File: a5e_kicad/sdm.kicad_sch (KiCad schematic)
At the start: 22 parts, among them U2 W25X20CLZP, U7 A5EB013B-B23B

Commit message: savegame
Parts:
- removed U2: W25X20CLZP, Package_SON:WSON-8-1EP_6x5mm_P1.27mm_EP3.4x4.3mm, symbol Memory_Flash:W25X20CLZP
- added U2: IS25WP256D-xM, Package_SO:SOIC-16W_7.5x10.3mm_P1.27mm, symbol Memory_Flash:IS25WP256D-xM
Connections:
- net 1V8: now also U2.2 (VCC)
- net GND: now also U2.10 (GND)
- net qspi_CLK: now also U2.16 (SCK)
- net qspi_D0: now also U2.15 (SI/IO0)
- net qspi_D1: now also U2.8 (SO/IO1)
- net qspi_D2: now also U2.9 (~{WP}/IO2)
- net qspi_D3: now also U2.1 (~{HOLD}/IO3)
- net ~{qspi_CS}: now also U2.7 (~{CE})
- net ~{qspi_rst_n}: now also U2.3 (~{RESET}/NC)

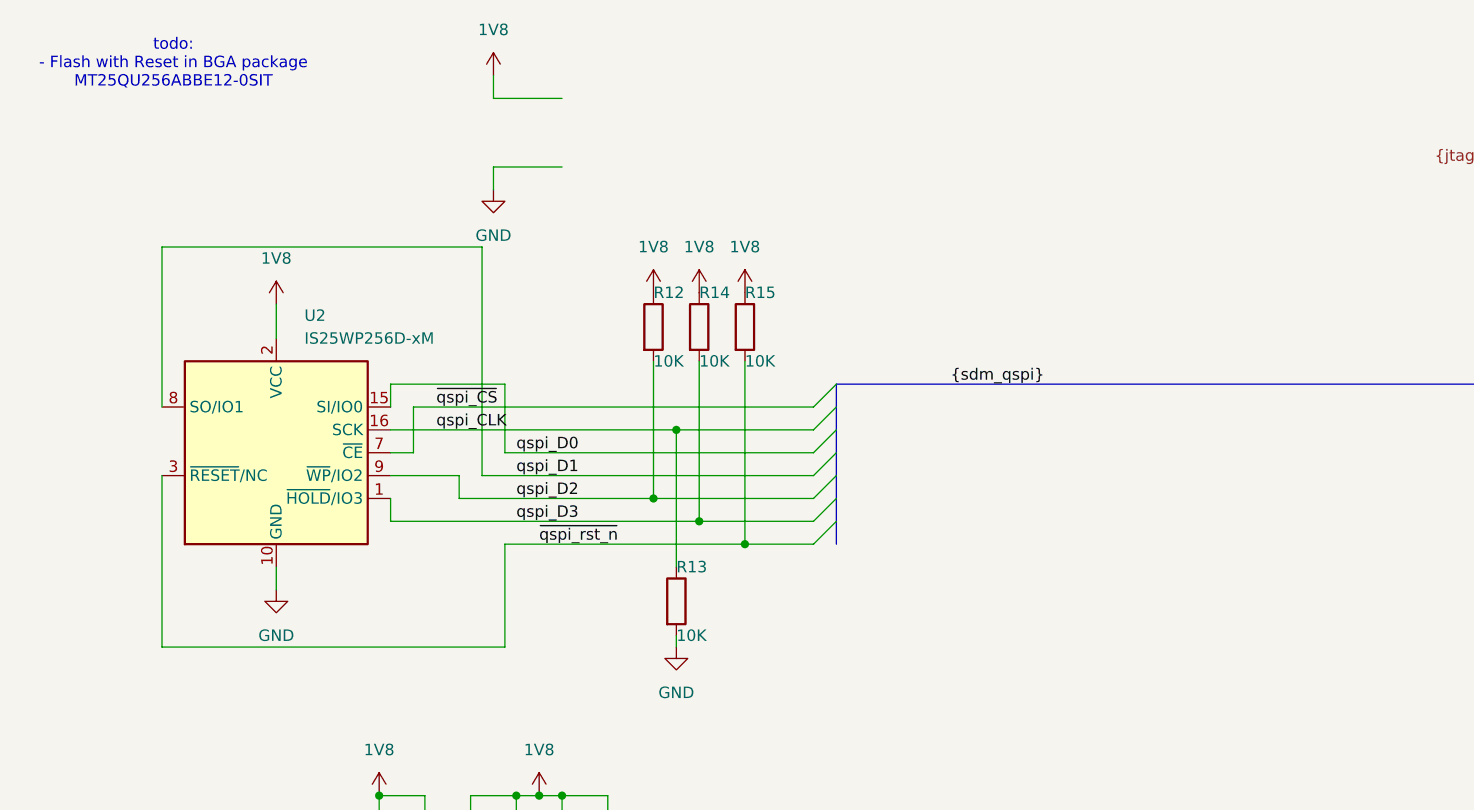
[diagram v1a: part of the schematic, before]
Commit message: change flash to correct part
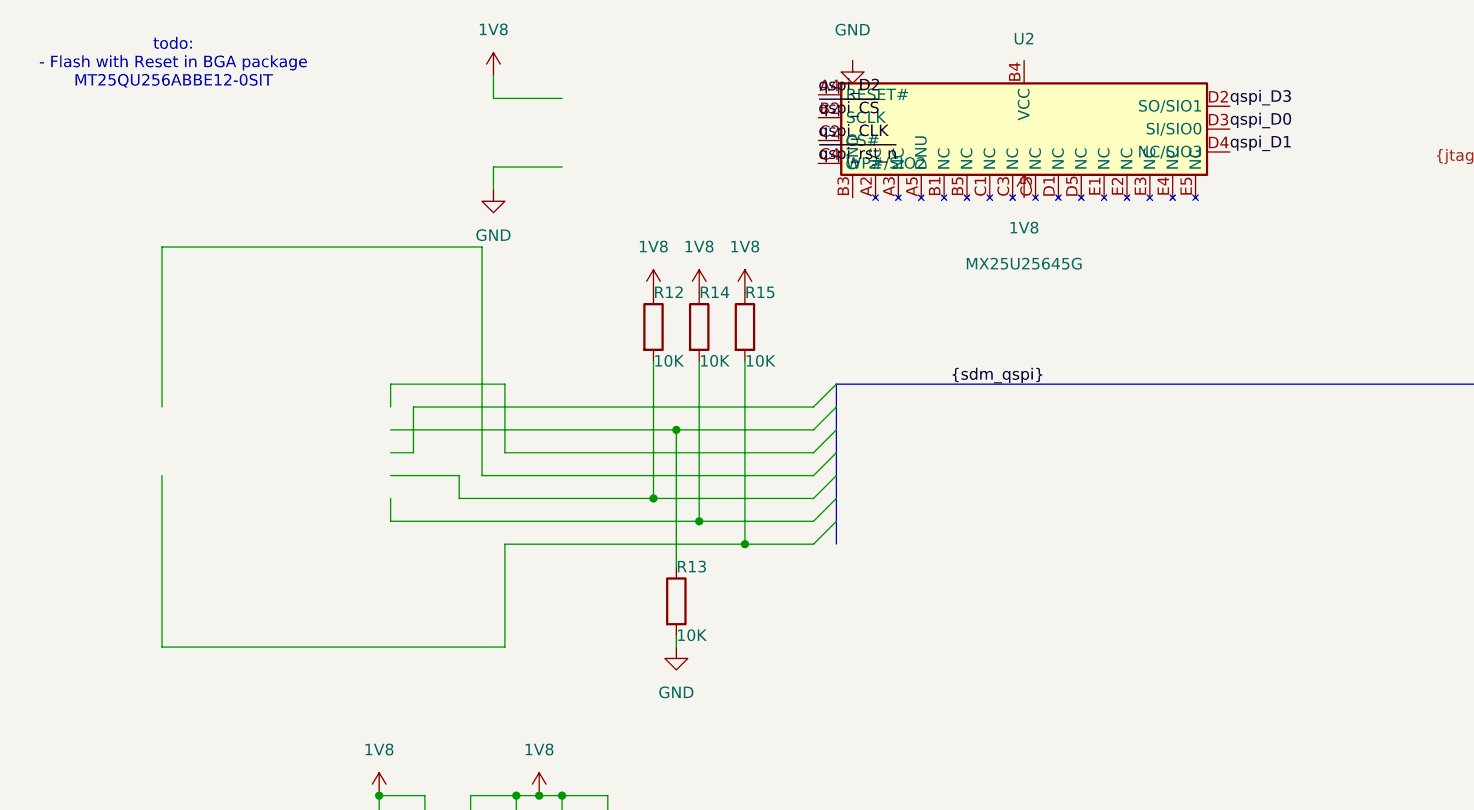
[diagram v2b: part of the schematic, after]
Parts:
- U2: value IS25WP256D-xM -> MX25U25645G; footprint Package_SO:SOIC-16W_7.5x10.3mm_P1.27mm -> agilex_lib:MX25U25645G_CSP24_6x8mm_P1.0mm; symbol Memory_Flash:IS25WP256D-xM -> agilex_5_lib:MX25U25645G
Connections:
- net 1V8: no longer U2.2 (VCC)
- net GND: no longer U2.10 (GND)
- net qspi_CLK: now also U2.C2 (CS#); no longer R13.1, U2.16 (SCK)
- net qspi_D0: now also U2.D3 (SI/SIO0); no longer U2.15 (SI/IO0)
- net qspi_D1: now also U2.D4 (NC/SIO3); no longer U2.8 (SO/IO1)
- net qspi_D2: now also U2.A4 (RESET#); no longer R12.2, U2.9 (~{WP}/IO2)
- net qspi_D3: now also U2.D2 (SO/SIO1); no longer R14.2, U2.1 (~{HOLD}/IO3)
- net ~{qspi_CS}: now also U2.B2 (SCLK); no longer U2.7 (~{CE})
- net ~{qspi_rst_n}: now also U2.C4 (WP#/SIO2); no longer R15.2, U2.3 (~{RESET}/NC)
